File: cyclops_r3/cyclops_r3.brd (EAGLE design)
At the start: 124.5 x 79.9 mm, 101 parts, among them Q1 BC817, Q2 IRF510, U1 MCP4921, U10 MCP4022, U2 317-N, U3 TLV3701, U4 337-N, U5 ADR03, U6 OP1177, U7 LTC2052HV, U8 ZXTD45

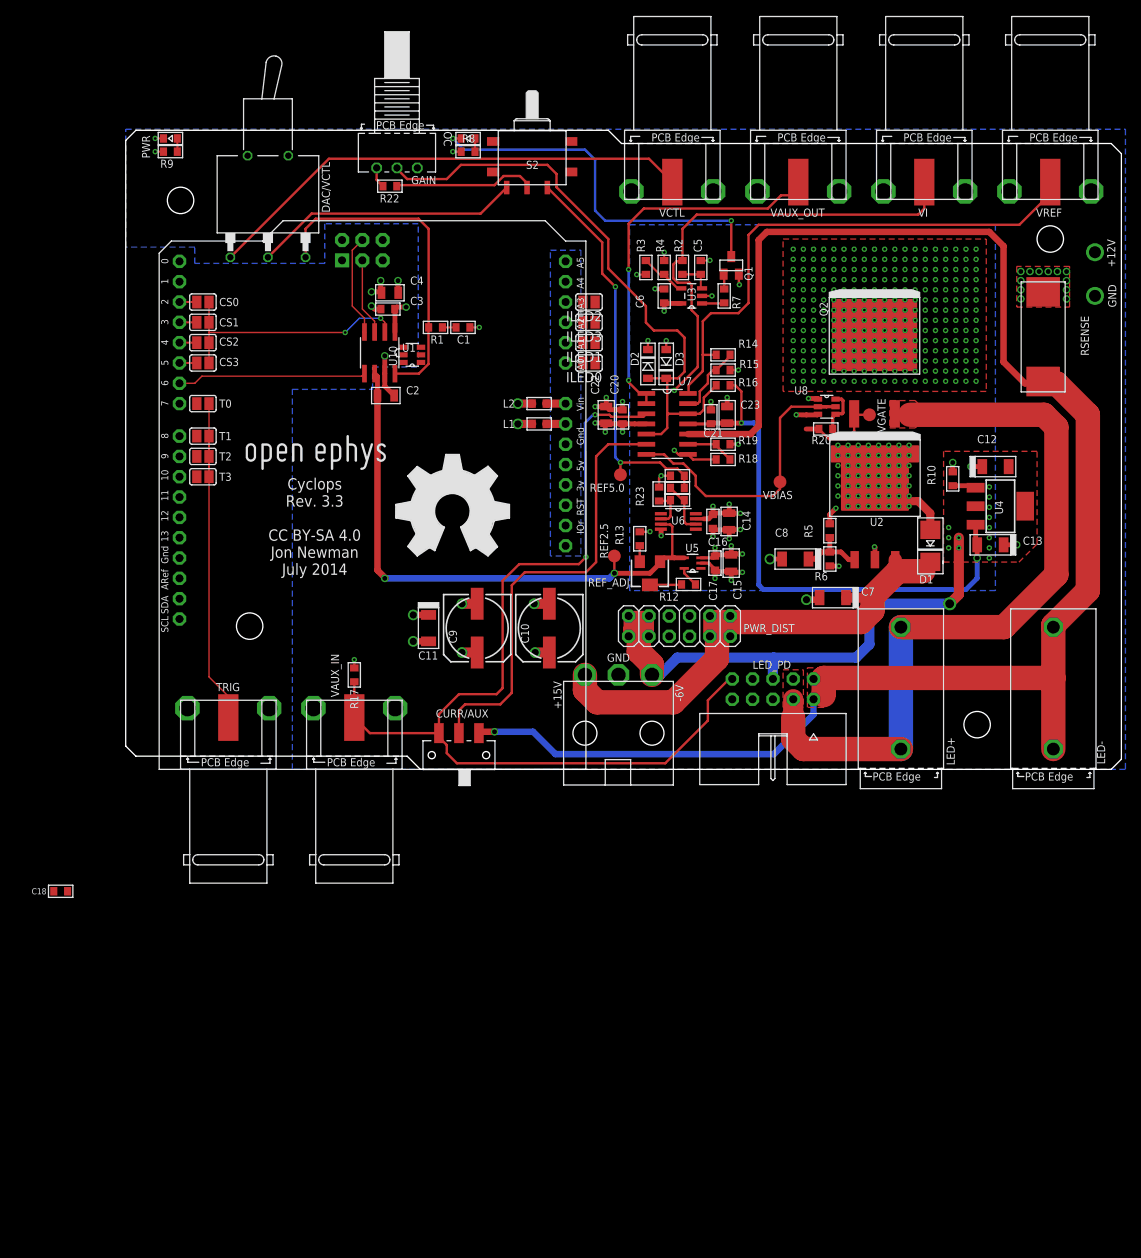
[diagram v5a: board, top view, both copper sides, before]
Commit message: Added digital overcurrent protection.
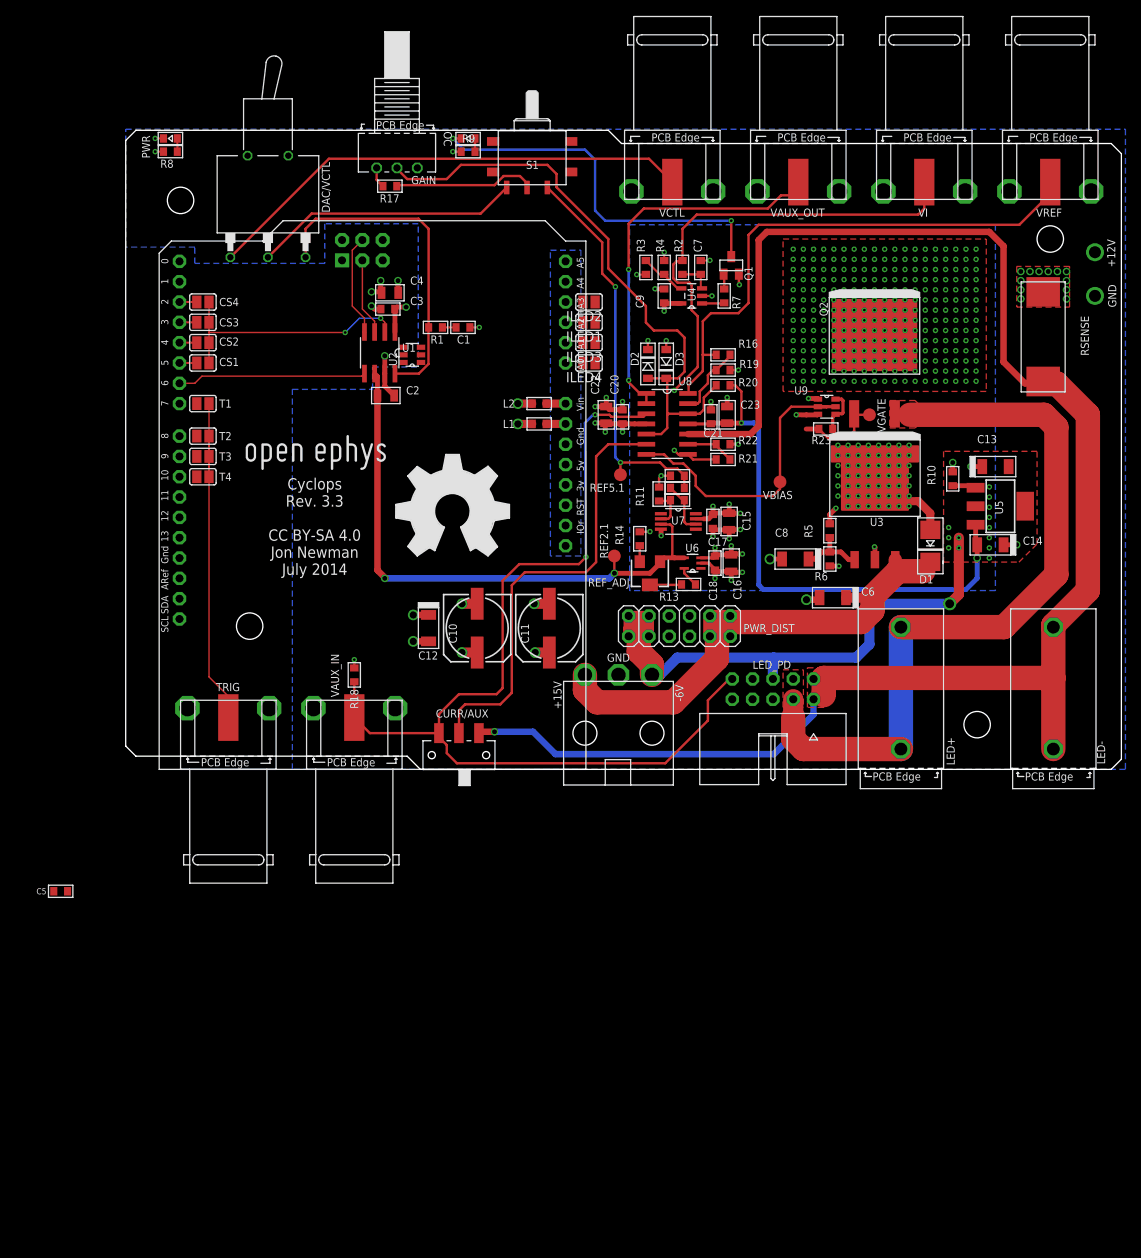
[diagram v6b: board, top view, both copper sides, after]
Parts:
- removed R24, R25: 1k, cyclops:0603
- removed T0: (no value), cyclops:SJ
- removed U10: MCP4022, cyclops:SOT23-6
- added R11, R21: 1k, cyclops:0603
- added T4: (no value), cyclops:SJ
- added U9: ZXTD45, cyclops:SOT23-6
- C11: value 1uF -> 100uF; device cyclops:1206-POL -> cyclops:153CLV-0807
- C14: device cyclops:0805 -> cyclops:1206-POL
- C16: value .1uF -> 1uF; device cyclops:0603 -> cyclops:0805
- C6: value .1uF -> 1uF; device cyclops:0603 -> cyclops:1206-POL
- C7: value 1uF -> .1uF; device cyclops:1206-POL -> cyclops:0603
- C9: value 100uF -> .1uF; device cyclops:153CLV-0807 -> cyclops:0603
- R12: value 470 -> 1k
- R13: value 1k -> 470
- R16: value 220k -> 1k
- R17: value 220k -> 5.6k DNP
- R18: value 1k -> 220k
- R20: value 10 -> 220k
- R22: value 5.6k DNP -> 1k
- R23: value 1k -> 10
- R8: value 1k -> 3k
- R9: value 3k -> 1k
- U2: value 317-N -> MCP4022; device cyclops:TO-263 -> cyclops:SOT23-6
- U3: value TLV3701 -> 317-N; device ti-extended:SOT95P280X145-5N -> cyclops:TO-263
- U4: value 337-N -> TLV3701; device cyclops:SOT223 -> ti-extended:SOT95P280X145-5N
- U5: value ADR03 -> 337-N; device cyclops:SOT65P210X110-5N -> cyclops:SOT223
- U6: value OP1177 -> ADR03; device cyclops:SOP65P490X110-8N -> cyclops:SOT65P210X110-5N
- U7: value LTC2052HV -> OP1177; device cyclops:SO14 -> cyclops:SOP65P490X110-8N
- U8: value ZXTD45 -> LTC2052HV; device cyclops:SOT23-6 -> cyclops:SO14
- moved C5 111.7 mm to (-8.13, -15.2), turned to 0 degrees
- moved C18 91.5 mm to (73.7, 25.8), turned to 270 degrees
- moved C12 73.7 mm to (37.9, 17.7), turned to 270 degrees
- moved R17 61.2 mm to (33.0, 72.9), turned to 0 degrees
- moved U2 60.7 mm to (35.8, 51.8), turned to 90 degrees
- moved R18 53.4 mm to (28.6, 11.8), turned to 90 degrees
- moved R22 52.7 mm to (74.7, 40.6)
- moved C9 47.7 mm to (67.3, 59.2), turned to 90 degrees
- moved U4 46.7 mm to (70.7, 59.2), turned to 180 degrees
- moved C7 44.5 mm to (71.9, 62.7), turned to 90 degrees
- moved C6 43.2 mm to (88.4, 21.5), turned to 180 degrees
- moved U5 39.1 mm to (109.3, 32.9), turned to 270 degrees
- moved R8 37.2 mm to (5.59, 77.2)
- moved R9 37.2 mm to (42.8, 77.2)
- moved U3 34.5 mm to (93.7, 33.4), turned to 0 degrees
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- renumbered C24 to C19, CS0 to CS4, ILED0 to ILED4, REF2.5 to REF2.1, REF5.0 to REF5.1, S2 to S1
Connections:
- removed net N$16: C18.1, U10.1
- removed net N$24: C18.2, U10.2
- net +11V: now also C12.+, C18.1, C9.1, R18.2, U3.2, U3.4, U4.5, U6.3, U7.7, U8.4, U9.1; no longer C14.1, C6.1, C9.+, R17.2, U2.2, U2.4, U3.5, U5.3, U6.7, U7.4, U8.1
- net +15V: now also C6.+, U3.3; no longer C7.+, U2.3
- net +5V: now also C5.1, U2.1
- net -1.25V: now also C14.-, R20.1, U5.3, U8.11; no longer C13.-, R16.1, U4.3, U7.11
- net -6V: now also C13.-, U5.4; no longer C12.-, U4.4
- net COMP+: now also C7.1, U4.3; no longer C5.1, U3.3
- net CS: now also U2.4; no longer U10.4
- net CS1: now also CS3.1; no longer CS1.1
- net CS3: now also CS1.1; no longer CS3.1
- net GND: now also C12.-, C14.+, C18.2, C6.-, C7.2, C9.2, R11.2, R14.1, R22.2, U2.2, U4.2, U6.2, U7.4, U9.3; no longer C12.+, C14.2, C6.2, C7.-, C9.-, R13.1, R15.2, R23.2, U3.2, U5.2, U6.4, U8.3
- net LED-: now also U8.10; no longer U7.10
- net N$10: now also R23.1, U9.4, U9.6; no longer R20.1, U8.4, U8.6
- net N$12: now also U5.1; no longer U4.1
- net N$13: now also R23.2; no longer R20.2
- net N$15: now also R21.1, R22.1, U8.9; no longer R18.1, R19.1, U7.9
- net N$18: now also R11.1, R12.2, U7.2; no longer R23.1, R24.2, U6.2
- net N$2: now also R9.1; no longer R8.1
- net N$20: now also R13.2, U6.5; no longer R12.2, U5.5
- net N$22: now also R13.1; no longer R12.1
- net N$27: now also U4.1; no longer U3.1
- net N$3: now also R8.1; no longer R9.1
- net N$4: now also U8.7, U9.2, U9.5; no longer U7.7, U8.2, U8.5
- net N$5: now also U4.4; no longer U3.4
- net N$6: now also R14.2; no longer R13.2
- net N$72: now also U3.1; no longer U2.1
- net N$8: now also R16.1, R19.1, U8.13; no longer R14.1, R15.1, U7.13
- net POT: now also U2.3; no longer U10.3
- net REF2.5: now also U6.4, U7.3; no longer U5.4, U6.3
- net REF5.0: now also R15.2; no longer R25.2
- net T0: now also T1.2; no longer T0.2
- net T1: now also T2.2; no longer T1.2
- net T2: now also T3.2; no longer T2.2
- net T3: now also T4.2; no longer T3.2
- net TRIG: now also T4.1; no longer T0.1
- net VAUX: now also R18.1, U8.3; no longer R17.1, U7.3
- net VAUX_OUT: now also U8.1, U8.2; no longer U7.1, U7.2
- net VCTL: now also R17.2, U2.6; no longer R22.2, U10.6
- net VCTL_PROTECT: now also R17.1, U2.5; no longer R22.1, U10.5
- net VFB: now also U8.6; no longer U7.6
- net VI: now also R21.2, U8.8; no longer R18.2, U7.8
- net VREF: now also R16.2, U8.14; no longer R14.2, U7.14
- net VREFA2X1: now also R12.1, R15.1, U7.6; no longer R24.1, R25.1, U6.6
- net _VREF: now also R20.2, U8.12, U8.5; no longer R16.2, U7.12, U7.5

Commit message: Added automatic overcurrent compenstation.
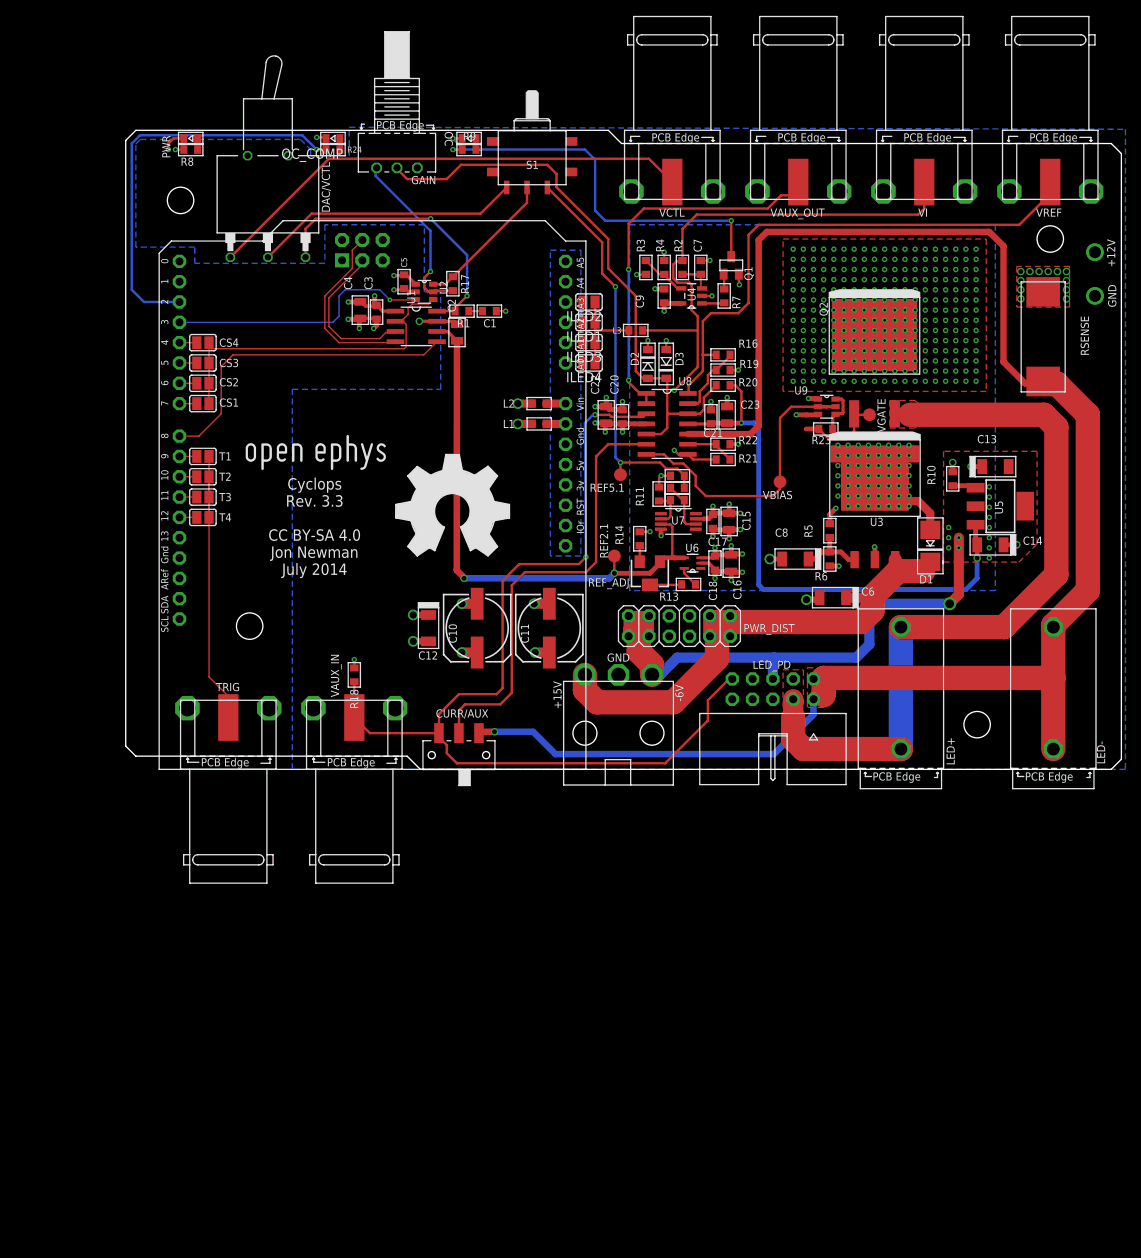
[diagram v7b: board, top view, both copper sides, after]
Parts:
- added L3: MPZ1608, cyclops:0603
- added OC_COMP: LEDRED, cyclops:LED-0603
- added R24: 1k, cyclops:0603
- U2: value MCP4022 -> MCP4022-50k
- moved C5 87.5 mm to (34.8, 61.0), turned to 270 degrees
- moved R17 14.5 mm to (40.9, 60.7), turned to 90 degrees
- moved C2 11.9 mm to (41.4, 54.6), turned to 90 degrees
- moved U2 8.02 mm to (37.3, 59.7), turned to 270 degrees
- moved T1 6.60 mm to (9.65, 39.1)
- moved U1 5.64 mm to (36.3, 55.4), turned to 270 degrees
- moved CS2 5.08 mm to (9.65, 48.3)
- moved CS3 5.08 mm to (9.65, 50.8)
- moved T4 5.08 mm to (9.65, 31.5)
- moved CS1 5.08 mm to (9.65, 45.7)
- moved CS4 5.08 mm to (9.65, 53.3)
- moved T2 5.08 mm to (9.65, 36.6)
- moved T3 5.08 mm to (9.65, 34.0)
- moved C4 4.28 mm to (29.3, 57.4), turned to 270 degrees
- moved C1 3.88 mm to (45.5, 57.3)
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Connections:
- new net N$16: OC_COMP.A, R24.1
- new net N$56: ILED1.1, ILED2.1, ILED3.1, ILED4.1, L3.1
- new net OC_COMP: LEONARDO.D2, R24.2
- net CS0: now also LEONARDO.D4; no longer LEONARDO.D2
- net CS1: now also LEONARDO.D5; no longer LEONARDO.D3
- net CS2: now also LEONARDO.D6; no longer LEONARDO.D4
- net CS3: now also LEONARDO.D7; no longer LEONARDO.D5
- net GND: now also OC_COMP.C
- net LDAC: now also LEONARDO.D8; no longer LEONARDO.D6
- net POT: now also LEONARDO.D3; no longer LEONARDO.D7
- net REF2.5: no longer LEONARDO.AREF
- net T0: now also LEONARDO.D9; no longer LEONARDO.D8
- net T1: now also LEONARDO.D10; no longer LEONARDO.D9
- net T2: now also LEONARDO.D11; no longer LEONARDO.D10
- net T3: now also LEONARDO.D12; no longer LEONARDO.D11
- net VI: now also L3.2; no longer ILED1.1, ILED2.1, ILED3.1, ILED4.1
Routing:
- net OC_COMP: track 0.00 -> 50.3 mm, vias 0 -> 1
- net GND: track 66.1 -> 112.1 mm, vias 52 -> 54
- net POT: track 0.00 -> 33.2 mm, vias 0 -> 1
- net VCTL_PROTECT: track 2.61 -> 22.0 mm, vias 0 -> 1
- net LDAC: track 23.7 -> 40.5 mm
- net N$56: track 0.00 -> 11.8 mm
- net CS: track 31.9 -> 42.4 mm, vias 2 -> 0
- net SDI: track 13.0 -> 22.9 mm
- net SCLK: track 9.59 -> 19.3 mm
- net VI: track 72.2 -> 79.1 mm
- net TRIG: track 45.3 -> 38.7 mm
- net DACA: track 41.6 -> 36.0 mm, vias 0 -> 2
- net _VREF: track 77.5 -> 72.4 mm
- net +5V: track 5.93 -> 10.9 mm, vias 2 -> 3
- net REF2.5: track 72.8 -> 69.8 mm
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
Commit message: Minor cleanup.
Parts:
- moved U$30 0.40 mm to (14.5, 37.3)
- renumbered OC_COMP to COMP
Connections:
- removed net N$11: L1.1, LEONARDO.GND2
- new net KEEPOUT_GND: L1.1, LEONARDO.GND2, LEONARDO.GND3
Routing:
- net N$11: track 2.43 -> 0.00 mm
- net KEEPOUT_GND: track 0.00 -> 2.43 mm
- added copper zone on layer 2, net KEEPOUT_GND
- removed copper zone on layer 2, net KEEPOUT
